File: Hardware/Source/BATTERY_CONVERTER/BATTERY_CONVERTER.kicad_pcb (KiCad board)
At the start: 2 copper layers, 100 x 79.3 mm, 65 parts, among them J1 BAT, J2 POWER_CONN, U1 LM5576MHX/NOPB, U2 TPS54331DR, U3 LD1117S33CTR_SOT223, U4 LD1117S33CTR_SOT223, U5 L7809CV, U6 ICL7662CBA

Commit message: pcb:bat_con:update pcb
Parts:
- moved C23 30.2 mm to (157.9, 54.5)
- moved C21 30.2 mm to (155.5, 52.5)
- moved C25 30.2 mm to (166.9, 62.8)
- moved C27 30.2 mm to (166.9, 63.2)
- moved U3 30.2 mm to (161.2, 58.5)
- moved R14 16.7 mm to (119.6, 110.4), turned to 180 degrees
- moved D4 14.6 mm to (118.3, 112.8), turned to 180 degrees
- moved C33 8.64 mm to (173.9, 83.8), turned to 0 degrees
- moved C34 5.29 mm to (180.6, 78.7), turned to 90 degrees
- moved D3 3.56 mm to (127.4, 107.6)
- moved J1 3.07 mm to (125.3, 112.3)
- moved U6 1.91 mm to (175.6, 77.8), turned to 90 degrees
- moved C28 0.42 mm to (153.1, 66.1)
- moved C22 0.42 mm to (144.1, 57.5)
- moved C24 0.42 mm to (141.7, 55.5)
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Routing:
- net GND: track 25.3 -> 128.1 mm, vias 5 -> 103
- net +5V: track 22.8 -> 93.2 mm
- net +3V3_O: track 13.2 -> 53.0 mm
- net +9V: track 6.52 -> 39.2 mm
- net -9V: track 0.00 -> 27.8 mm
- net +3V3: track 13.2 -> 29.0 mm
- net +12V: track 195.7 -> 185.6 mm
- net +BATT: track 37.7 -> 41.2 mm
- net Net-(U6-CAP+): track 0.00 -> 2.26 mm
- net Net-(U6-CAP-): track 0.00 -> 2.25 mm
- net Net-(D4-A): track 0.00 -> 1.76 mm
- net Net-(U2-EN): track 7.13 -> 6.62 mm
- added copper zone on B.Cu, net GND
- added copper zone on F.Cu, net GND
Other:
- board size 100 x 79.3 mm -> 100 x 78.4 mm
- board text added: "+5V"
- board text added: "+9V"
- board text added: "+BAT"
- board text added: "-9V"
- board text added: "-BAT"
- board text added: "3V3"
- board text added: "GND"

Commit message: update bat
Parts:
- removed the C4 at (147.3, 102.5)
- moved C3 7.35 mm to (145.3, 103.5)
- renumbered C11 to C10, C12 to C11, C13 to C12, C14 to C13, C15 to C14, C16 to C15, C17 to C16, C18 to C17, C19 to C18, C20 to C19, C21 to C20, C22 to C21, C23 to C22, C24 to C23, C25 to C24, C26 to C25, C27 to C26, C28 to C27, C29 to C28, C30 to C29, C31 to C30, C32 to C31, C33 to C32, C34 to C33, C5 to C4, C6 to C5, C7 to C6, C8 to C7, C9 to C8, C10 to C9
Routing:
- net +BATT: track 41.2 -> 36.4 mm
- net Net-(U2-VSENSE): track 8.85 -> 8.15 mm
- net GND: vias 103 -> 100

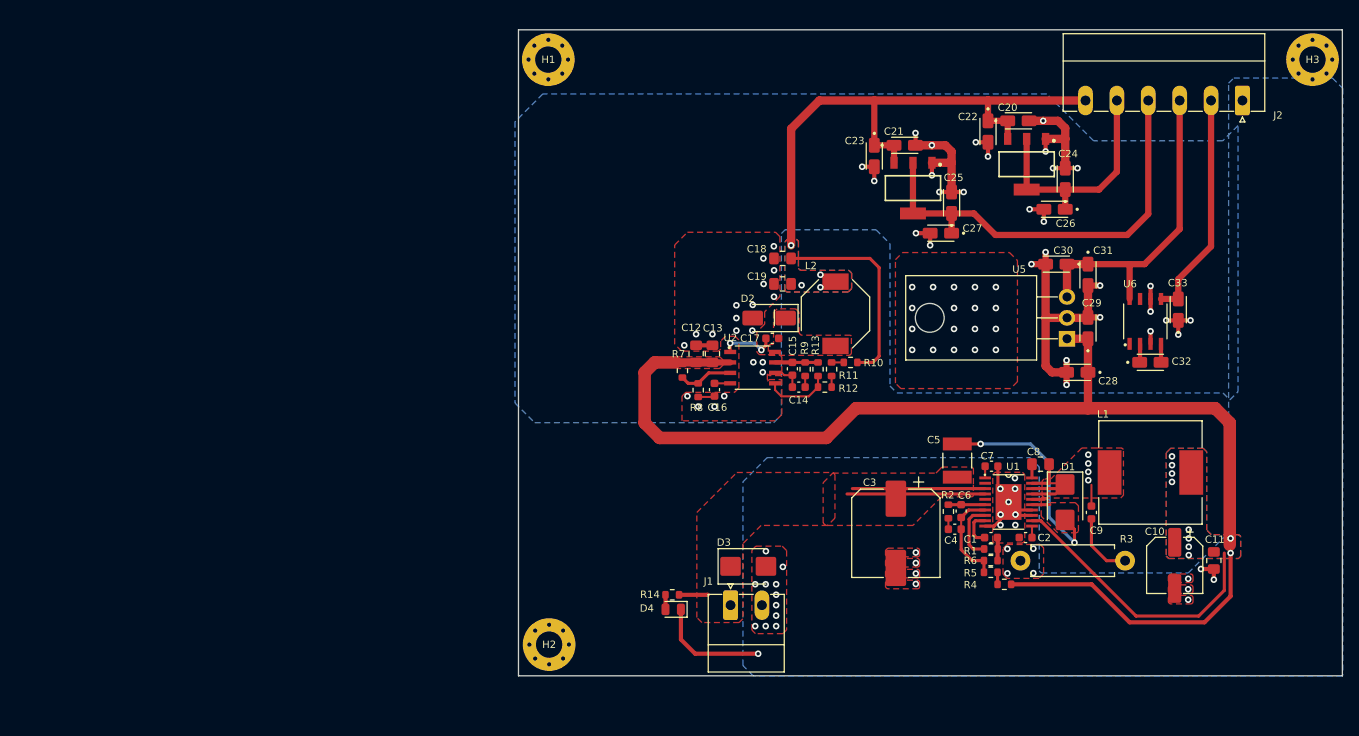
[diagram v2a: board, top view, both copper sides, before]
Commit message: Export Gerber file except Powersupply
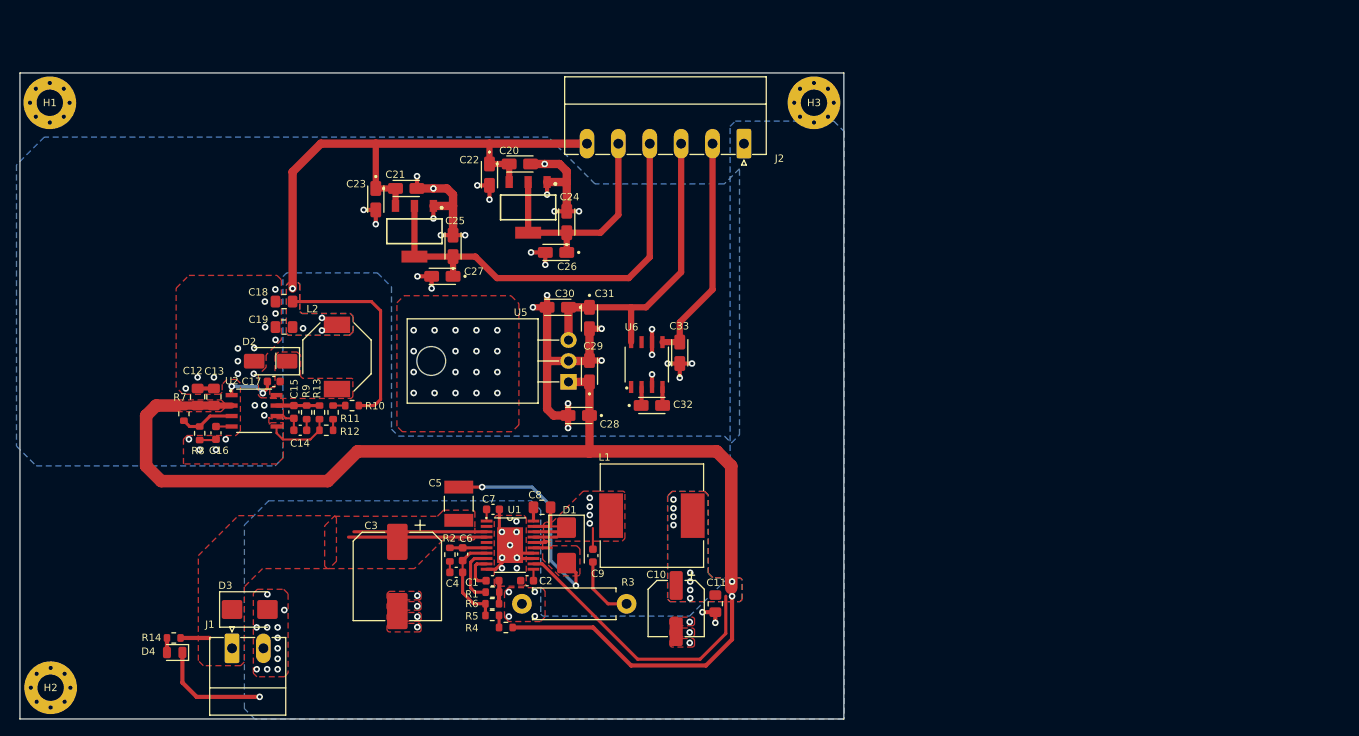
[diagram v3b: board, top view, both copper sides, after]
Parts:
- moved C18 60.7 mm to (71.1, 75.5)
- moved C19 60.7 mm to (71.1, 78.6)
- moved C21 60.7 mm to (83.6, 62.7)
- moved C22 60.7 mm to (97.4, 59.7)
- moved C28 60.7 mm to (109.2, 88.2)
- moved C29 60.7 mm to (109.2, 86.2)
- moved C31 60.7 mm to (107.2, 75.1)
- moved C32 60.7 mm to (113.4, 89.0)
- moved C33 60.7 mm to (120.1, 83.9)
- moved C6 60.7 mm to (92.8, 106.1)
- moved C9 60.7 mm to (108.6, 106.3)
- moved D1 60.7 mm to (105.4, 105.0)
- moved H2 60.7 mm to (42.7, 122.3)
- moved J1 60.7 mm to (64.8, 117.5)
- moved L1 60.7 mm to (115.7, 101.4)
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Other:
- board text added: "BOARD GUIDELINE"
- board text added: "Layer stackup: 1. Top Layer 2. Bottom Layer"
- board text added: "Note: 1. Board dimension: 100mmx78.41mm 2. 2 Layer 3. 1.6mm thickness 4. Silkscreen using white 5. Solder mask: Green"
- board text added: "Top silkscreen Top soldermask Top Layer Bottom Layer Bottom soldermask Bottom silkscreen"
